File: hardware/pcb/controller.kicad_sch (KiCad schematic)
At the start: 14 parts, among them J2 Conn_02x13_Odd_Even, U3 ESP32-WROOM-32E

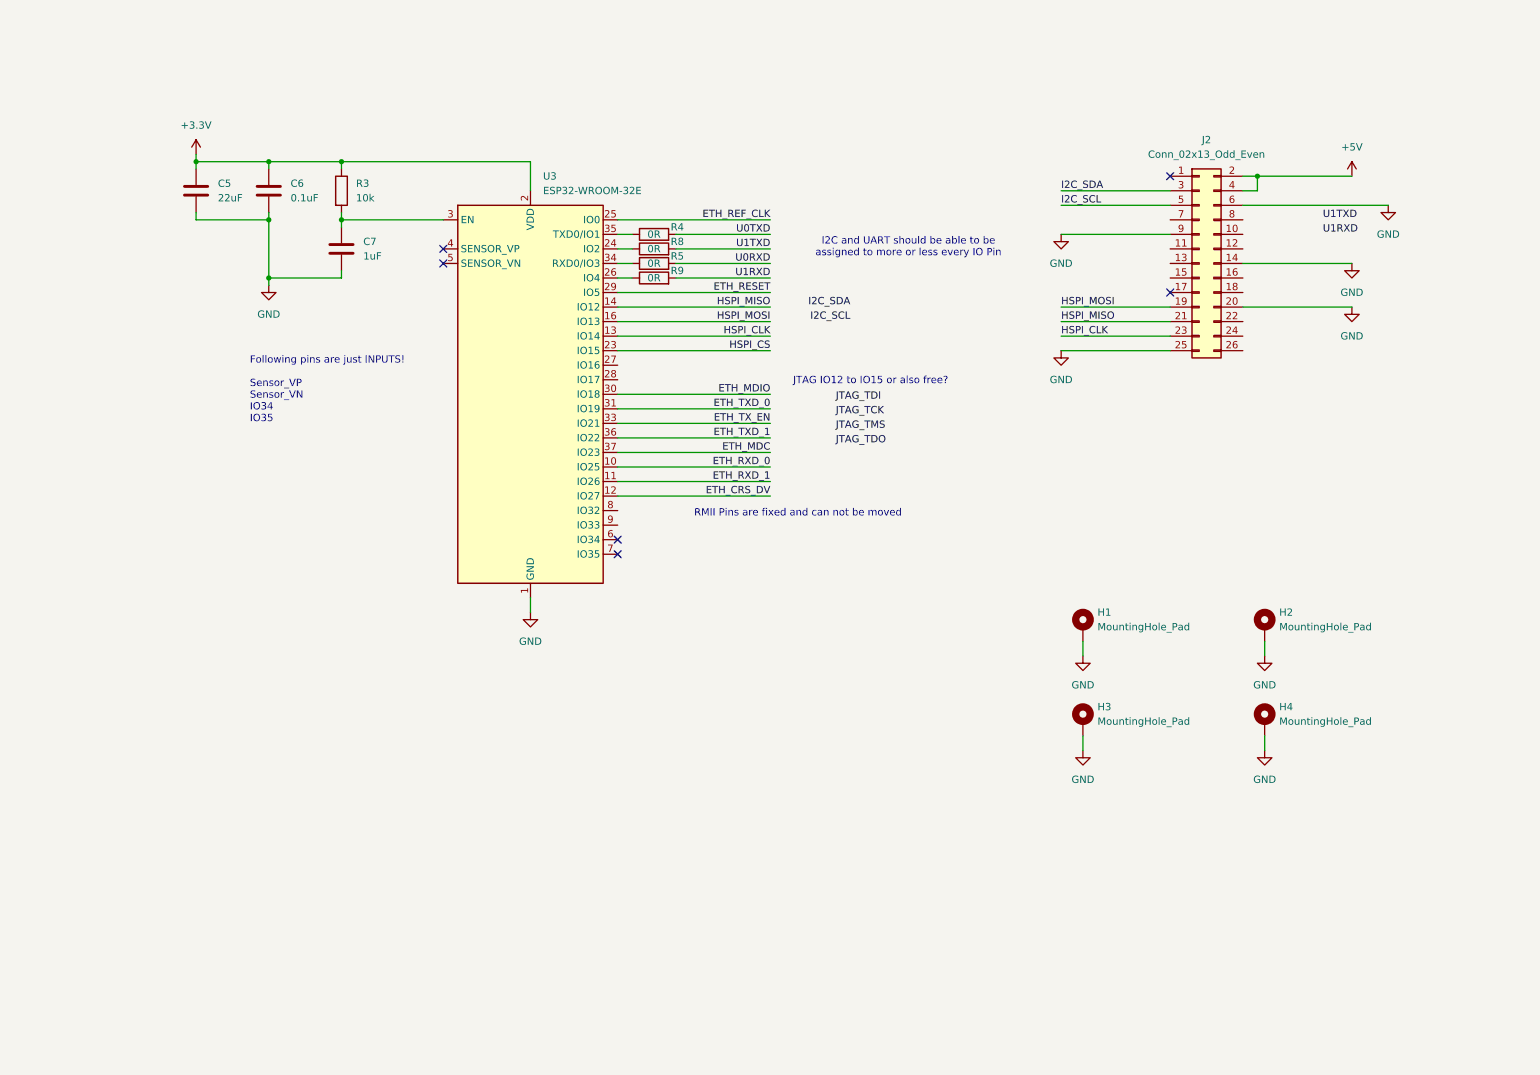
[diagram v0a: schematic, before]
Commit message: draft: Added USB UART interface
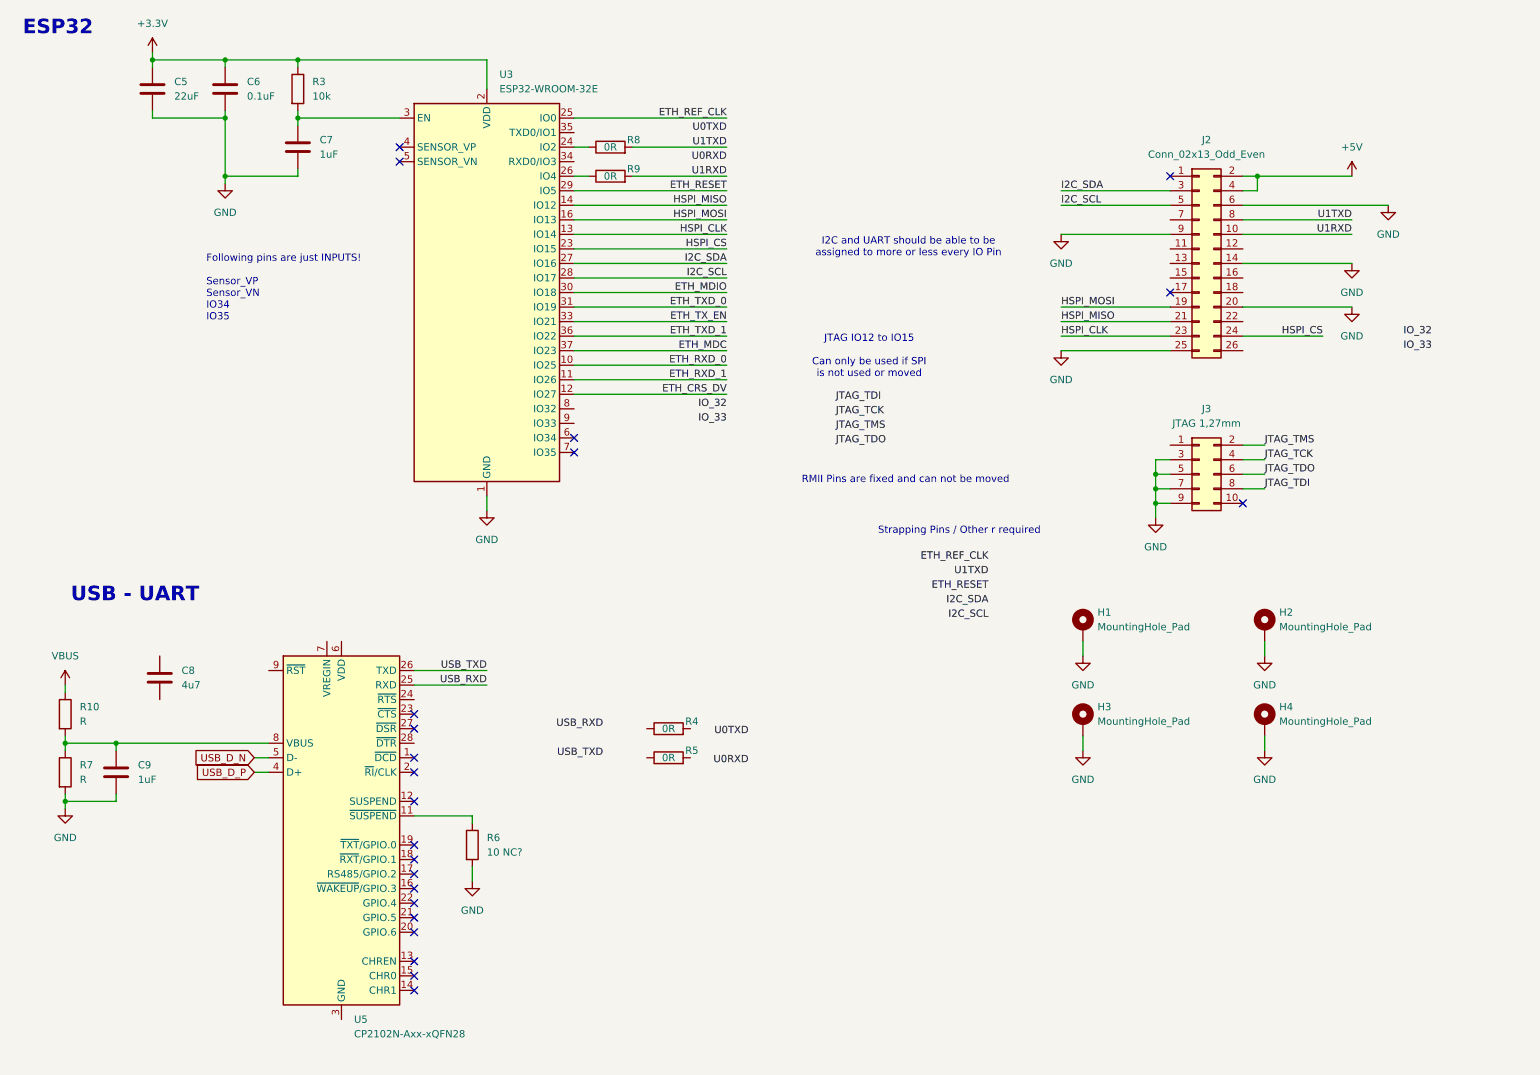
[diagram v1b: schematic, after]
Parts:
- added C8: 4u7, symbol Device:C
- added C9: 1uF, symbol Device:C
- added J3: JTAG 1,27mm, symbol Connector_Generic:Conn_02x05_Odd_Even
- added R10, R7: R, symbol Device:R
- added R6: 10 NC?, symbol Device:R
- added U5: CP2102N-Axx-xQFN28, Package_DFN_QFN:QFN-28-1EP_5x5mm_P0.5mm_EP3.35x3.35mm, symbol Interface_USB:CP2102N-Axx-xQFN28
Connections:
- net GND: now also C9.2, J3.3 (Pin_3), J3.5 (Pin_5), J3.7 (Pin_7), J3.9 (Pin_9), R6.2, R7.2
- net HSPI_CS: now also J2.24 (Pin_24)
- net I2C_SCL: now also U3.28 (IO17)
- net I2C_SDA: now also U3.27 (IO16)
- net JTAG_TCK: now also J3.4 (Pin_4)
- net JTAG_TDI: now also J3.8 (Pin_8)
- net JTAG_TDO: now also J3.6 (Pin_6)
- net JTAG_TMS: now also J3.2 (Pin_2)
- net U0RXD: no longer R5.2
- net U0TXD: no longer R4.2
- net U1RXD: now also J2.10 (Pin_10)
- net U1TXD: now also J2.8 (Pin_8)
- net at R5.1: no longer U3.34 (RXD0/IO3)
- net at R4.1: no longer U3.35 (TXD0/IO1)
- new net: C9.1, R10.2, R7.1, U5.8 (VBUS)
- new net: R6.1, U5.11 (~{SUSPEND})
- new net: U5.29 (GND), U5.3 (GND)
- new net USB_D_N: U5.5 (D-)
- new net USB_D_P: U5.4 (D+)
- new net USB_RXD: U5.25 (RXD)
- new net USB_TXD: U5.26 (TXD)
- new net VBUS: R10.1
- no-connect marks 6 -> 22
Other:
- note added: "ESP32"
- note added: "JTAG IO12 to IO15 Can only be used if SPI is not used or moved"
- note added: "Strapping Pins / Other r required"
- note added: "USB - UART"
- note removed: "JTAG IO12 to IO15 or also free?"
- moved on the sheet: C5, C6, C7, R3, R4, R5, R8, R9, U3

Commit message: draft: High level overview
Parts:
- added C10: 0u1, symbol Device:C
- added R11: 1K, symbol Device:R
- R10: value R -> 22,1K (1%)
- R7: value R -> 47,5k
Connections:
- net +3.3V: now also C8.1, U5.6 (VDD), U5.7 (VREGIN), C10.1, R11.1
- net GND: now also C8.2, C10.2
- net U0RXD: now also R5.2
- net U0TXD: now also R4.2
- net USB_RXD: now also R4.1
- net USB_TXD: now also R5.1
- net at U5.9 (~{RST}): now also R11.2
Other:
- note added: "Auto program"
- moved on the sheet: C8, R4, R5

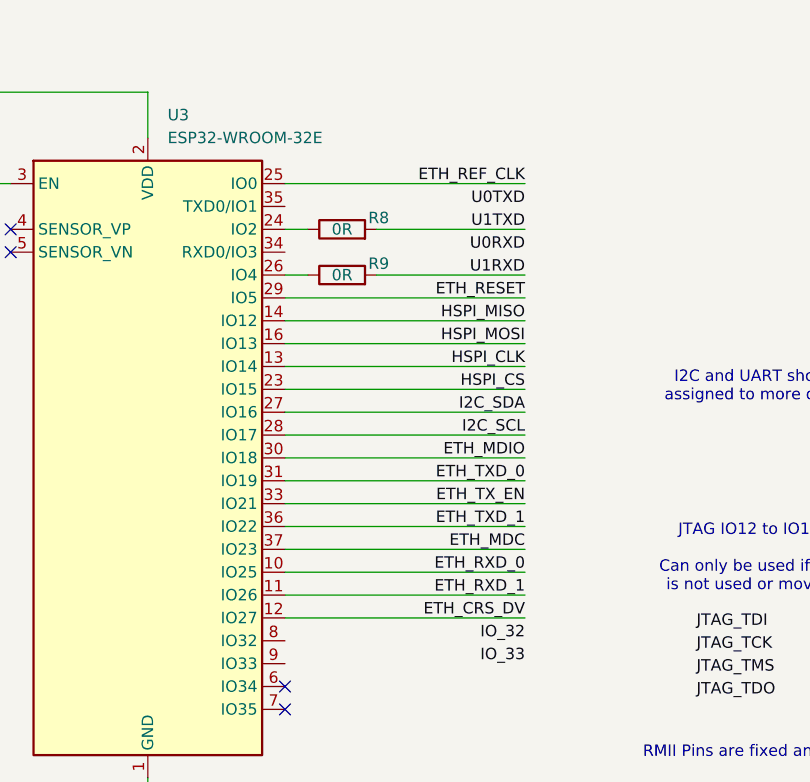
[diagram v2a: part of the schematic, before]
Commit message: draft: Added W5500 Ethernet
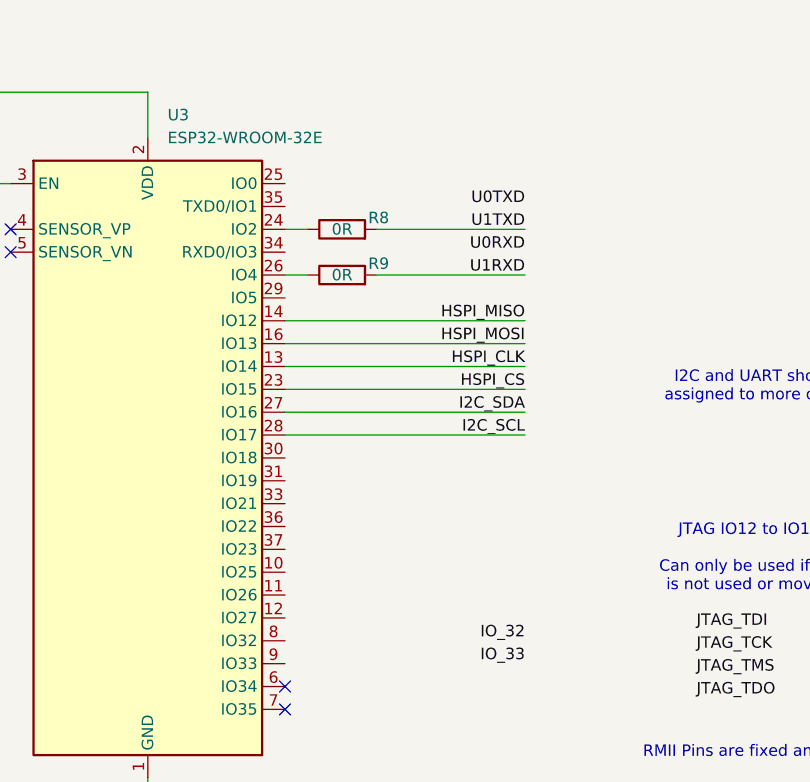
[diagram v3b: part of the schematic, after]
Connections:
- net ETH_REF_CLK: no longer U3.25 (IO0)
- net ETH_RESET: no longer U3.29 (IO5)
- net ETH_CRS_DV: no longer names the net of U3.12 (IO27)
- net ETH_MDC: no longer names the net of U3.37 (IO23)
- net ETH_MDIO: no longer names the net of U3.30 (IO18)
- net ETH_RXD_0: no longer names the net of U3.10 (IO25)
- net ETH_RXD_1: no longer names the net of U3.11 (IO26)
- net ETH_TXD_0: no longer names the net of U3.31 (IO19)
- net ETH_TXD_1: no longer names the net of U3.36 (IO22)
- net ETH_TX_EN: no longer names the net of U3.33 (IO21)
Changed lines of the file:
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@@
-	(wire
-		(pts
-			(xy 118.11 78.74) (xy 144.78 78.74)
-		)
-		(stroke
-			(width 0)
-			(type default)
-		)
-	)
 	(wire
 		(pts
@@
 	(wire
 		(pts
-			(xy 118.11 48.26) (xy 144.78 48.26)
-		)
-		(stroke
-			(width 0)
-			(type default)
-		)
-	)
-	(wire
-		(pts
 			(xy 234.95 73.66) (xy 248.92 73.66)
 		)
@@
 	(wire
 		(pts
-			(xy 118.11 71.12) (xy 144.78 71.12)
-		)
-		(stroke
-			(width 0)
-			(type default)
-		)
-	)
-	(wire
-		(pts
 			(xy 36.83 124.46) (xy 46.99 124.46)
 		)
@@
 	(wire
 		(pts
-			(xy 118.11 68.58) (xy 144.78 68.58)
-		)
-		(stroke
-			(width 0)
-			(type default)
-		)
-	)
-	(wire
-		(pts
 			(xy 237.49 45.72) (xy 237.49 48.26)
 		)
@@
 	(wire
 		(pts
-			(xy 118.11 81.28) (xy 144.78 81.28)
-		)
-		(stroke
-			(width 0)
-			(type default)
-		)
-	)
-	(wire
-		(pts
 			(xy 123.19 142.24) (xy 125.73 142.24)
 		)
@@
 	(wire
 		(pts
-			(xy 118.11 83.82) (xy 144.78 83.82)
-		)
-		(stroke
-			(width 0)
-			(type default)
-		)
-	)
-	(wire
-		(pts
 			(xy 128.27 45.72) (xy 144.78 45.72)
 		)
@@
 	(wire
 		(pts
-			(xy 118.11 76.2) (xy 144.78 76.2)
-		)
-		(stroke
-			(width 0)
-			(type default)
-		)
-	)
-	(wire
-		(pts
 			(xy 69.85 25.4) (xy 69.85 26.67)
 		)
@@
 	(wire
 		(pts
-			(xy 118.11 73.66) (xy 144.78 73.66)
-		)
-		(stroke
-			(width 0)
-			(type default)
-		)
-	)
-	(wire
-		(pts
 			(xy 46.99 114.3) (xy 36.83 114.3)
 		)
@@
 	(wire
 		(pts
-			(xy 118.11 35.56) (xy 144.78 35.56)
-		)
-		(stroke
-			(width 0)
-			(type default)
-		)
-	)
-	(wire
-		(pts
 			(xy 234.95 45.72) (xy 237.49 45.72)
 		)
@@
 		(pts
 			(xy 69.85 44.45) (xy 69.85 45.72)
-		)
-		(stroke
-			(width 0)
-			(type default)
-		)
-	)
-	(wire
-		(pts
-			(xy 118.11 66.04) (xy 144.78 66.04)
 		)
 		(stroke
@@
 		)
 	)
-	(label "ETH_RESET"
-		(at 144.78 48.26 180)
-		(fields_autoplaced yes)
-		(effects
-			(font
-				(size 1.27 1.27)
-			)
-			(justify right bottom)
-		)
-	)
 	(label "USB_TXD"
 		(at 123.19 149.86 180)
@@
 		)
 	)
-	(label "ETH_MDC"
-		(at 144.78 76.2 180)
-		(fields_autoplaced yes)
-		(effects
-			(font
-				(size 1.27 1.27)
-			)
-			(justify right bottom)
-		)
-	)
 	(label "U0TXD"
 		(at 137.16 142.24 0)
@@
 		)
 	)
-	(label "ETH_TX_EN"
-		(at 144.78 71.12 180)
-		(fields_autoplaced yes)
-		(effects
-			(font
-				(size 1.27 1.27)
-			)
-			(justify right bottom)
-		)
-	)
 	(label "JTAG_TMS"
 		(at 238.76 92.71 0)
@@
 		)
 	)
-	(label "ETH_RXD_0"
-		(at 144.78 78.74 180)
-		(fields_autoplaced yes)
-		(effects
-			(font
-				(size 1.27 1.27)
-			)
-			(justify right bottom)
-		)
-	)
 	(label "HSPI_CLK"
 		(at 203.2 73.66 0)
@@
 		)
 	)
-	(label "ETH_MDIO"
-		(at 144.78 66.04 180)
-		(fields_autoplaced yes)
-		(effects
-			(font
-				(size 1.27 1.27)
-			)
-			(justify right bottom)
-		)
-	)
 	(label "ETH_REF_CLK"
 		(at 190.5 113.03 180)
@@
 		)
 	)
-	(label "ETH_TXD_0"
-		(at 144.78 68.58 180)
-		(fields_autoplaced yes)
-		(effects
-			(font
-				(size 1.27 1.27)
-			)
-			(justify right bottom)
-		)
-	)
 	(label "U0TXD"
 		(at 144.78 38.1 180)
@@
 		)
 	)
-	(label "ETH_CRS_DV"
-		(at 144.78 83.82 180)
-		(fields_autoplaced yes)
-		(effects
-			(font
-				(size 1.27 1.27)
-			)
-			(justify right bottom)
-		)
-	)
 	(label "U0RXD"
 		(at 137.16 149.86 0)
@@
 		)
 	)
-	(label "ETH_REF_CLK"
-		(at 144.78 35.56 180)
-		(fields_autoplaced yes)
-		(effects
-			(font
-				(size 1.27 1.27)
-			)
-			(justify right bottom)
-		)
-	)
 	(label "USB_RXD"
 		(at 102.87 134.62 180)
@@
 		)
 	)
-	(label "ETH_TXD_1"
-		(at 144.78 73.66 180)
-		(fields_autoplaced yes)
-		(effects
-			(font
-				(size 1.27 1.27)
-			)
-			(justify right bottom)
-		)
-	)
 	(label "I2C_SDA"
 		(at 203.2 48.26 0)
@@
 		)
 	)
-	(label "ETH_RXD_1"
-		(at 144.78 81.28 180)
-		(fields_autoplaced yes)
-		(effects
-			(font
-				(size 1.27 1.27)
-			)
-			(justify right bottom)
-		)
-	)
